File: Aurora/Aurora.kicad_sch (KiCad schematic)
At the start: 32 parts, among them J1 UJ20-C-H-C-3-SMT-TR, U1 STM32H757BITx, U2 USBLC6-2SC6

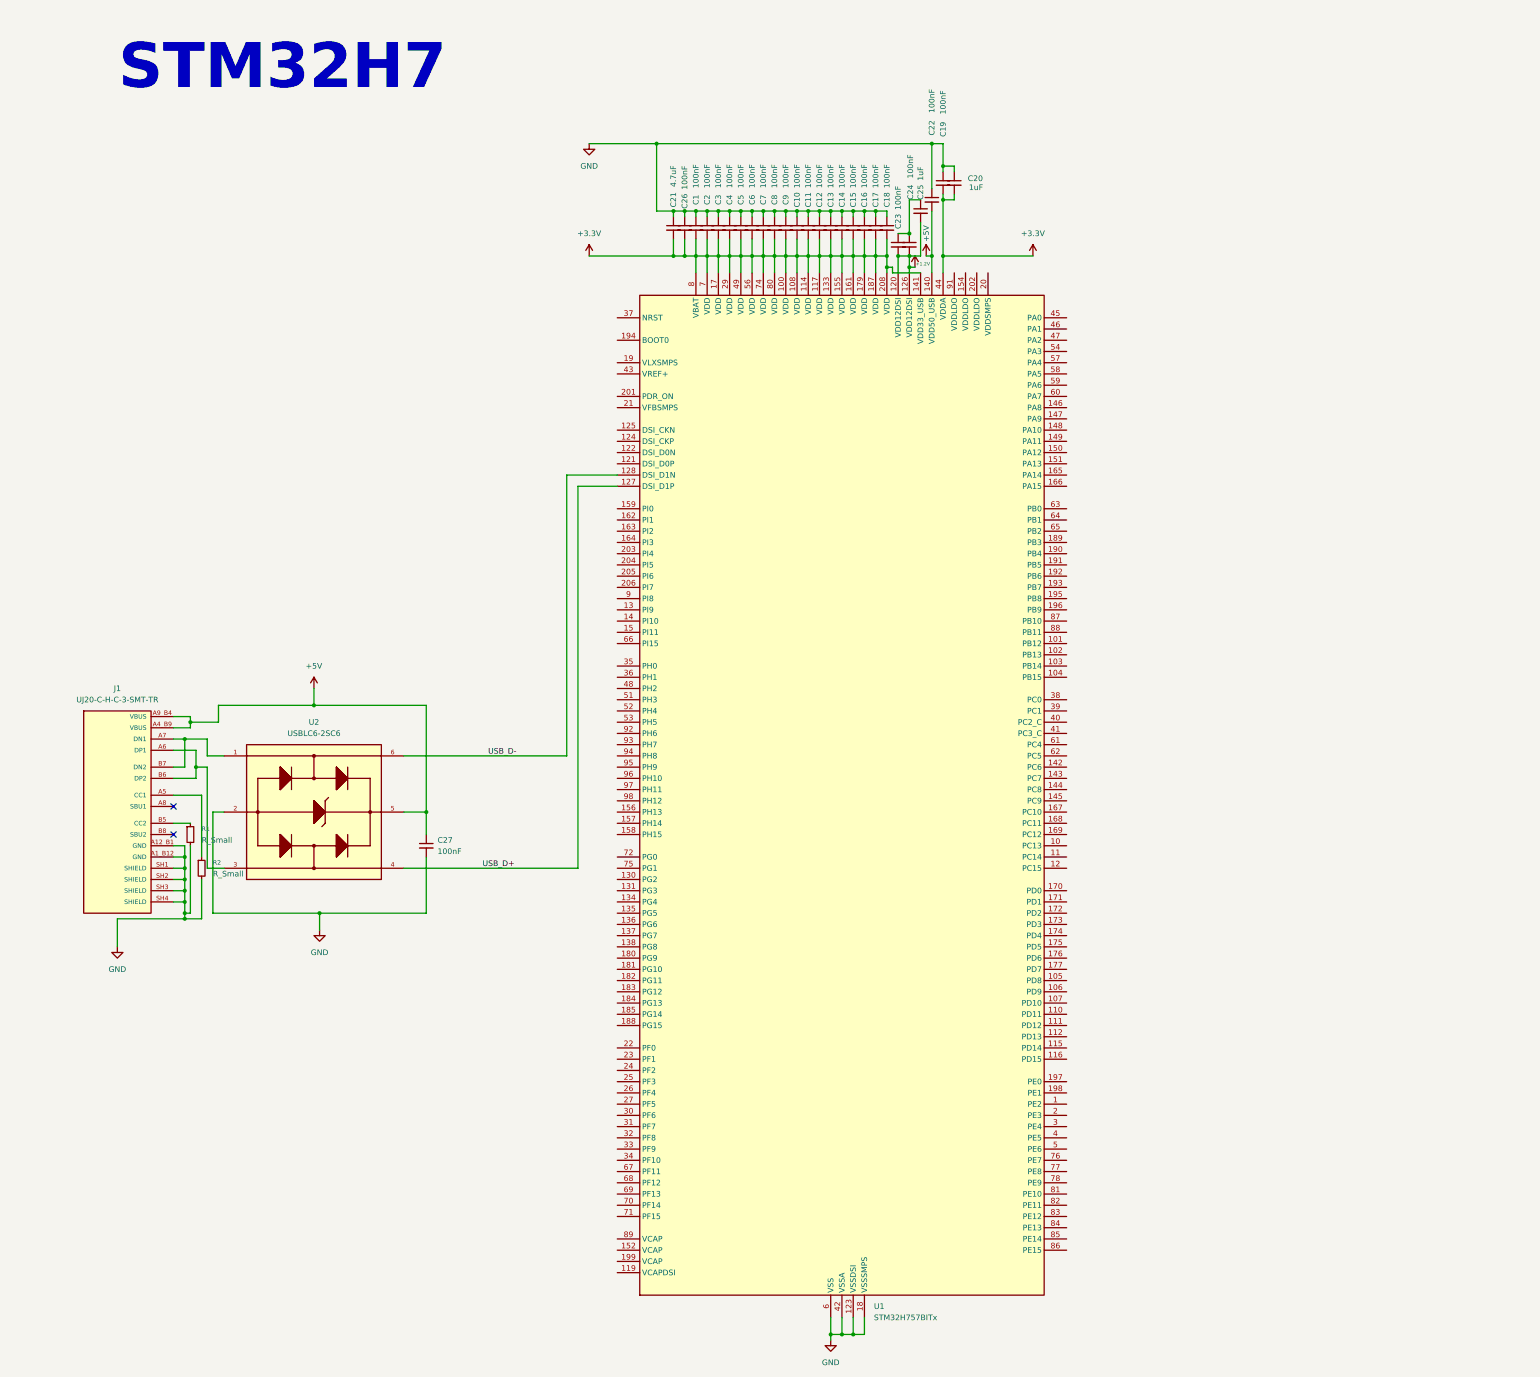
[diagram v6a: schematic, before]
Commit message: Voltage regulator, some comments
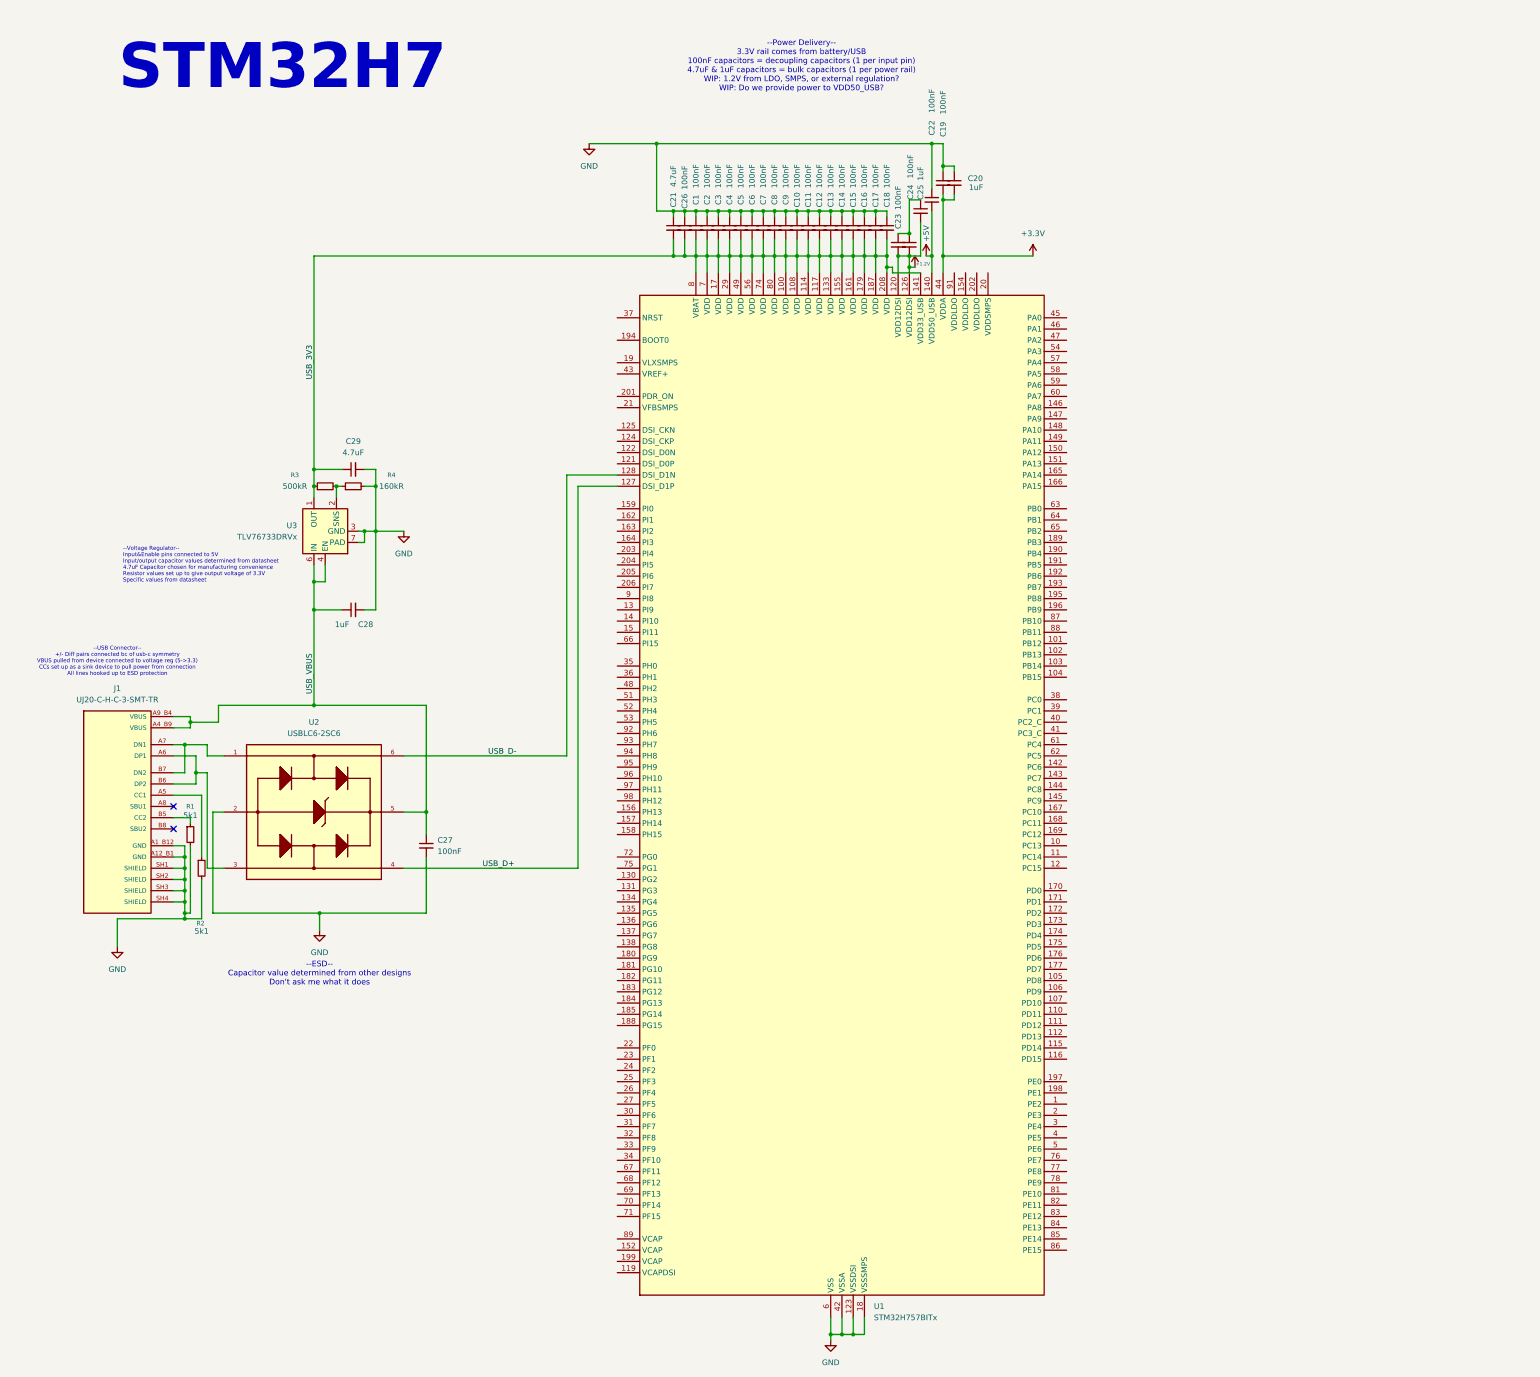
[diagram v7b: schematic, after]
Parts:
- added C28: 1uF, symbol Device:C_Small
- added C29: 4.7uF, symbol Device:C_Small
- added R3: 500kR, symbol Device:R_Small
- added R4: 160kR, symbol Device:R_Small
- added U3: TLV76733DRVx, Package_SON:WSON-6-1EP_2x2mm_P0.65mm_EP1x1.6mm_ThermalVias, symbol Regulator_Linear:TLV76733DRVx
- J1: footprint UJ20-C-H-C-3-SMT-TR:CUI_UJ20-C-H-C-3-SMT-TR -> UJ20-C-H-C-3-SMT-TR (1):CUI_UJ20-C-H-C-3-SMT-TR
- R1, R2: value R_Small -> 5k1
- U2: footprint USBLC6-2SC6:SOT95P280X145-6N -> USBLC6_2SC6:SOT95P280X145-6N
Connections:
- net +3.3V: no longer C1.2, C10.2, C11.2, C12.2, C13.2, C14.2, C15.2, C16.2, C17.2, C18.2, C2.2, C21.2, C26.2, C3.2, C4.2, C5.2, C6.2, C7.2, C8.2, C9.2, U1.100 (VDD), U1.108 (VDD), U1.114 (VDD), U1.117 (VDD), U1.133 (VDD), U1.141 (VDD33_USB), U1.155 (VDD), U1.161 (VDD), U1.17 (VDD), U1.179 (VDD), U1.187 (VDD), U1.208 (VDD), U1.29 (VDD), U1.49 (VDD), U1.56 (VDD), U1.7 (VDD), U1.74 (VDD), U1.8 (VBAT), U1.80 (VDD)
- net +5V: no longer C27.1, J1.A4_B9 (VBUS), J1.A9_B4 (VBUS), U2.5
- net GND: now also C28.2, C29.2, R4.2, U3.3 (GND), U3.5 (GND), U3.7 (PAD)
- new net: R3.2, R4.1, U3.2 (SNS)
- new net USB_3V3: C1.2, C10.2, C11.2, C12.2, C13.2, C14.2, C15.2, C16.2, C17.2, C18.2, C2.2, C21.2, C26.2, C29.1, C3.2, C4.2, C5.2, C6.2, C7.2, C8.2, C9.2, R3.1, U1.100 (VDD), U1.108 (VDD), U1.114 (VDD), U1.117 (VDD), U1.133 (VDD), U1.141 (VDD33_USB), U1.155 (VDD), U1.161 (VDD), U1.17 (VDD), U1.179 (VDD), U1.187 (VDD), U1.208 (VDD), U1.29 (VDD), U1.49 (VDD), U1.56 (VDD), U1.7 (VDD), U1.74 (VDD), U1.8 (VBAT), U1.80 (VDD), U3.1 (OUT)
- new net USB_VBUS: C27.1, C28.1, J1.A4_B9 (VBUS), J1.A9_B4 (VBUS), U2.5, U3.4 (EN), U3.6 (IN)
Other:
- note added: "--ESD-- Capacitor value determined from other designs Don't ask me what it does"
- note added: "--Power Delivery-- 3.3V rail comes from battery/USB 100nF capacitors = decoupling capacitors (1 per input pin) 4.7uF & 1uF capacitors = bulk capacitors (1 per power rail) WIP: 1.2V from LDO, SMPS, or external regulation? WIP: Do we provide power to VDD50_USB?"
- note added: "--USB Connector-- +/- Diff pairs connected bc of usb-c symmetry VBUS pulled from device connected to voltage reg (5->3.3) CCs set up as a sink device to pull power from connection All lines hooked up to ESD protection"
- note added: "--Voltage Regulator-- Input&Enable pins connected to 5V Input/output capacitor values determined from datasheet 4.7uF Capacitor chosen for manufacturing convenience Resistor values set up to give output voltage of 3.3V Specific values from datasheet"

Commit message: ICM and other sensors
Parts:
- added Barometer-(U7): BMP390L, BMP390L:XDCR_BMP390L, symbol BMP390L:BMP390L
- added Micro-SD-Socket-(J2): MSD4-3-A, MSD4-3-A:CUI_MSD4-3-A, symbol MSD4-3-A:MSD4-3-A
- added U4: ICM-45686, ICM-45686:IC_ICM-45686, symbol ICM-45686:ICM-45686
- added U5: ICM-42688-P, ICM-42688-P:PQFN50P300X250X97-14N, symbol ICM-42688-P:ICM-42688-P
- added U6: BNO085, BNO085:IC_BNO085, symbol BNO085:BNO085
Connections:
- new net: U6.1 (RESV_NC), U6.12 (RESV_NC), U6.13 (RESV_NC), U6.21 (RESV_NC), U6.22 (RESV_NC), U6.23 (RESV_NC), U6.24 (RESV_NC), U6.7 (RESV_NC), U6.8 (RESV_NC)
- new net: Barometer-(U7).3 (VSS/GND), Barometer-(U7).8 (VSS/GND), Barometer-(U7).9 (VSS/GND)
